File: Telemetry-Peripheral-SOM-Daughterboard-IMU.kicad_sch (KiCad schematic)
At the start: 8 parts, among them J1 Conn_02x10_Odd_Even, U1 LSM6DSV

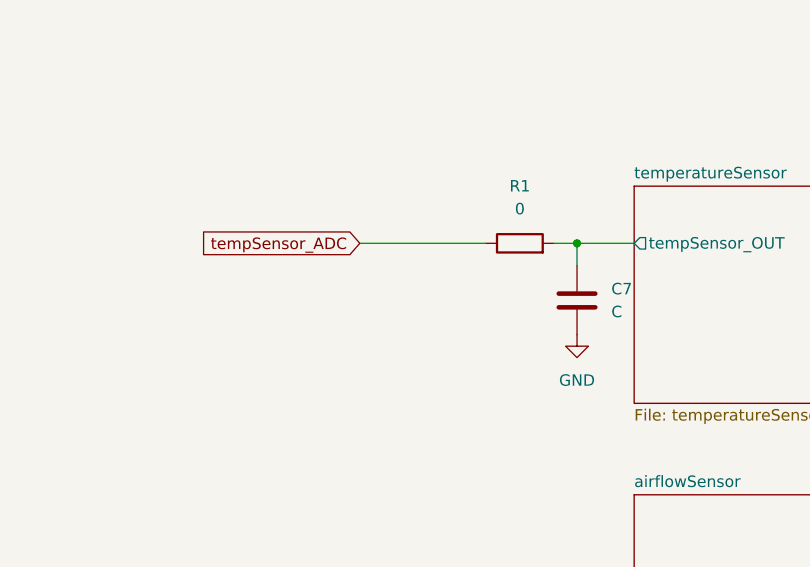
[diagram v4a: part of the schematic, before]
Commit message: temperatureSensor fix
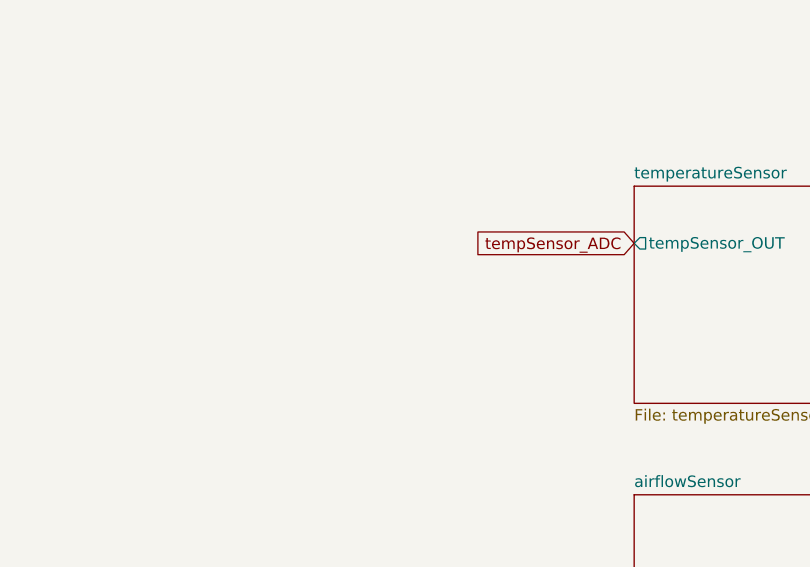
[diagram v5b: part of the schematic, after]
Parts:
- removed C7: C, symbol Device:C
- removed R1: 0, symbol Device:R
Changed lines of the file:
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@@
   (junction (at 87.63 40.64) (diameter 0) (color 0 0 0 0)
-  )
-  (junction (at 119.38 127) (diameter 0) (color 0 0 0 0)
   )
   (junction (at 80.01 38.1) (diameter 0) (color 0 0 0 0)
@@
     (stroke (width 0) (type default))
   )
-  (wire (pts (xy 119.38 127) (xy 119.38 129.54))
-    (stroke (width 0) (type default))
-  )
   (wire (pts (xy 254 45.72) (xy 257.81 45.72))
     (stroke (width 0) (type default))
@@
     (stroke (width 0) (type default))
   )
-  (wire (pts (xy 116.84 127) (xy 119.38 127))
-    (stroke (width 0) (type default))
-  )
   (wire (pts (xy 254 30.48) (xy 257.81 30.48))
     (stroke (width 0) (type default))
@@
   )
   (wire (pts (xy 254 43.18) (xy 257.81 43.18))
-    (stroke (width 0) (type default))
-  )
-  (wire (pts (xy 95.25 127) (xy 109.22 127))
-    (stroke (width 0) (type default))
-  )
-  (wire (pts (xy 119.38 127) (xy 125.73 127))
     (stroke (width 0) (type default))
   )
@@
     (effects (font (size 1.27 1.27)) (justify right bottom))
   )
-  (global_label "tempSensor_ADC" (shape input) (at 95.25 127 180) (fields_autoplaced)
+  (global_label "tempSensor_ADC" (shape input) (at 125.73 127 180) (fields_autoplaced)
     (effects (font (size 1.27 1.27)) (justify right))
-    (property "Intersheetrefs" "${INTERSHEET_REFS}" (at 76.6016 127 0)
+    (property "Intersheetrefs" "${INTERSHEET_REFS}" (at 107.0816 127 0)
       (effects (font (size 1.27 1.27)) (justify right) hide)
     )
@@
         (path "/d5ebd247-5a7c-47c2-8aee-beabaef72d6d"
           (reference "#PWR043") (unit 1)
-        )
-      )
-    )
-  )
-  (symbol (lib_id "Device:C") (at 119.38 133.35 0) (unit 1)
-    (in_bom yes) (on_board yes) (dnp no) (fields_autoplaced)
-    (property "Reference" "C7" (at 123.19 132.08 0)
-      (effects (font (size 1.27 1.27)) (justify left))
-    )
-    (property "Value" "C" (at 123.19 134.62 0)
-      (effects (font (size 1.27 1.27)) (justify left))
-    )
-    (property "Footprint" "" (at 120.3452 137.16 0)
-      (effects (font (size 1.27 1.27)) hide)
-    )
-    (property "Datasheet" "~" (at 119.38 133.35 0)
-      (effects (font (size 1.27 1.27)) hide)
-    )
-    (pin "1")
-    (pin "2")
-    (instances
-      (project "Telemetry-Peripheral-SOM-Daughterboard-IMU"
-        (path "/637f68f0-cb9c-412a-8573-5d8e7ef6d8a2"
-          (reference "C7") (unit 1)
         )
       )
@@
     )
   )
-  (symbol (lib_id "power:GND") (at 119.38 137.16 0) (unit 1)
-    (in_bom yes) (on_board yes) (dnp no) (fields_autoplaced)
-    (property "Reference" "#PWR017" (at 119.38 143.51 0)
-      (effects (font (size 1.27 1.27)) hide)
-    )
-    (property "Value" "GND" (at 119.38 142.24 0)
-      (effects (font (size 1.27 1.27)))
-    )
-    (property "Footprint" "" (at 119.38 137.16 0)
-      (effects (font (size 1.27 1.27)) hide)
-    )
-    (property "Datasheet" "" (at 119.38 137.16 0)
-      (effects (font (size 1.27 1.27)) hide)
-    )
-    (pin "1")
-    (instances
-      (project "Telemetry-Peripheral-SOM-Daughterboard-IMU"
-        (path "/637f68f0-cb9c-412a-8573-5d8e7ef6d8a2"
-          (reference "#PWR017") (unit 1)
-        )
-      )
-    )
-  )
   (symbol (lib_id "Device:C_Small") (at 80.01 41.91 0) (unit 1)
     (in_bom yes) (on_board yes) (dnp no)
@@
         )
       )
-    )
-  )
-  (symbol (lib_id "Device:R") (at 113.03 127 90) (unit 1)
-    (in_bom yes) (on_board yes) (dnp no) (fields_autoplaced)
-    (property "Reference" "R1" (at 113.03 120.65 90)
-      (effects (font (size 1.27 1.27)))
-    )
-    (property "Value" "0" (at 113.03 123.19 90)
-      (effects (font (size 1.27 1.27)))
-    )
-    (property "Footprint" "" (at 113.03 128.778 90)
-      (effects (font (size 1.27 1.27)) hide)
-    )
-    (property "Datasheet" "~" (at 113.03 127 0)
-      (effects (font (size 1.27 1.27)) hide)
-    )
-    (pin "1")
-    (pin "2")
-    (instances
-      (project "Telemetry-Peripheral-SOM-Daughterboard-IMU"
-        (path "/637f68f0-cb9c-412a-8573-5d8e7ef6d8a2"
-          (reference "R1") (unit 1)
-        )
-      )

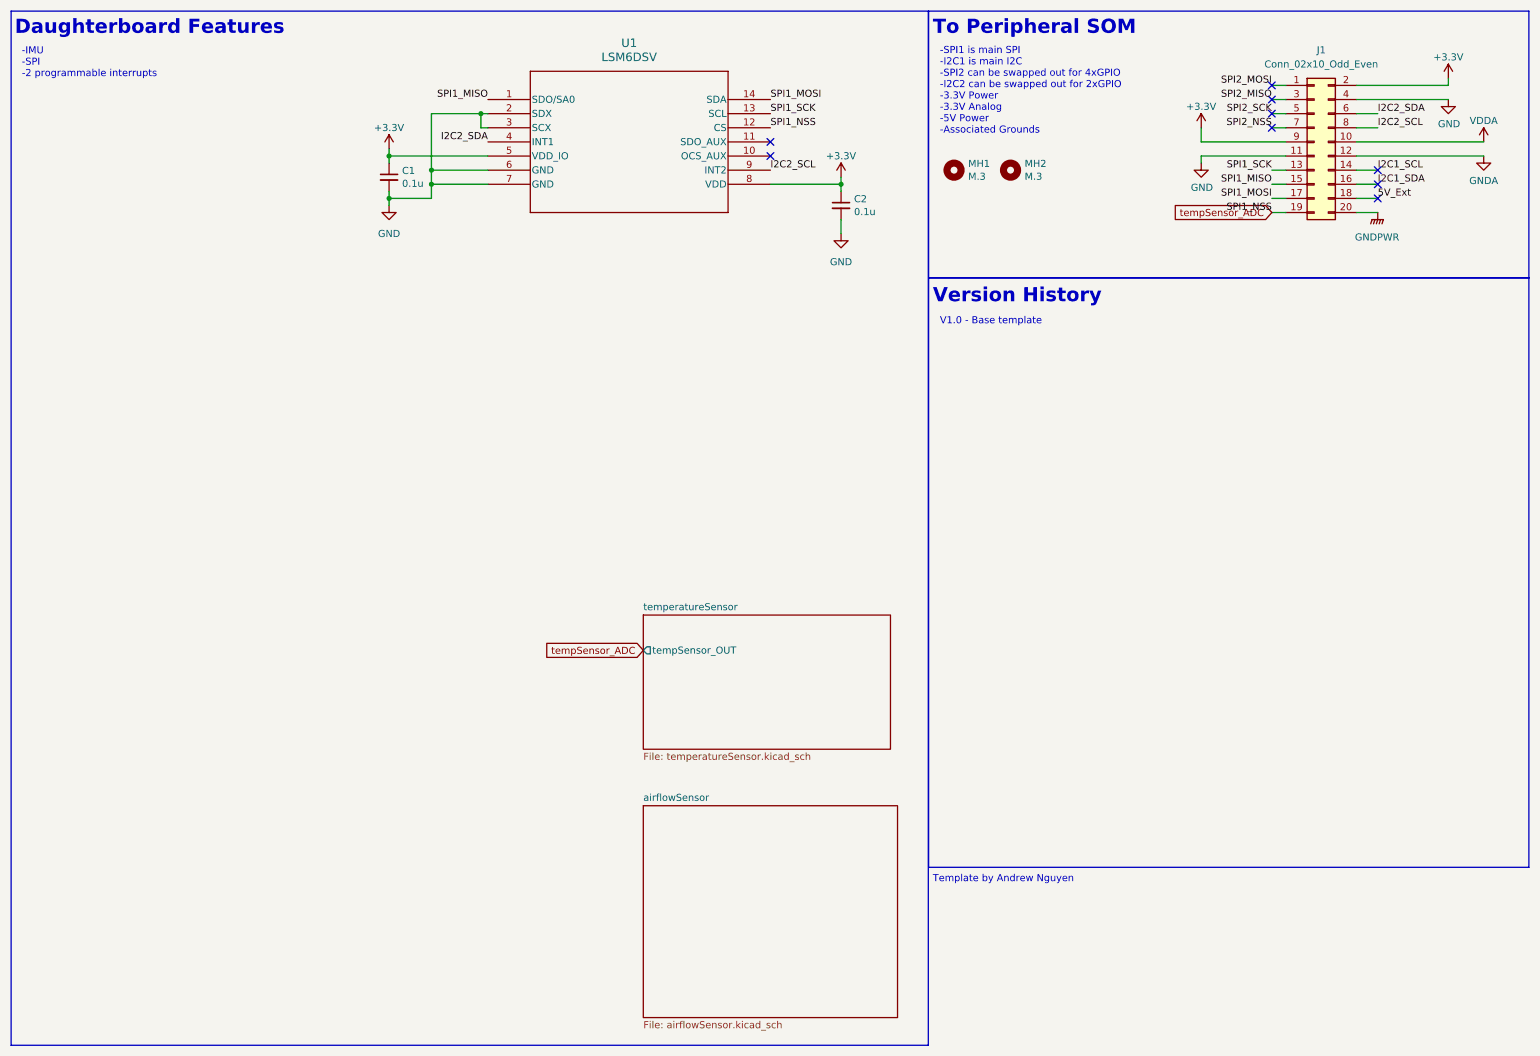
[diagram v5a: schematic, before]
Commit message: connected airflow and temperature sensors to connector J1
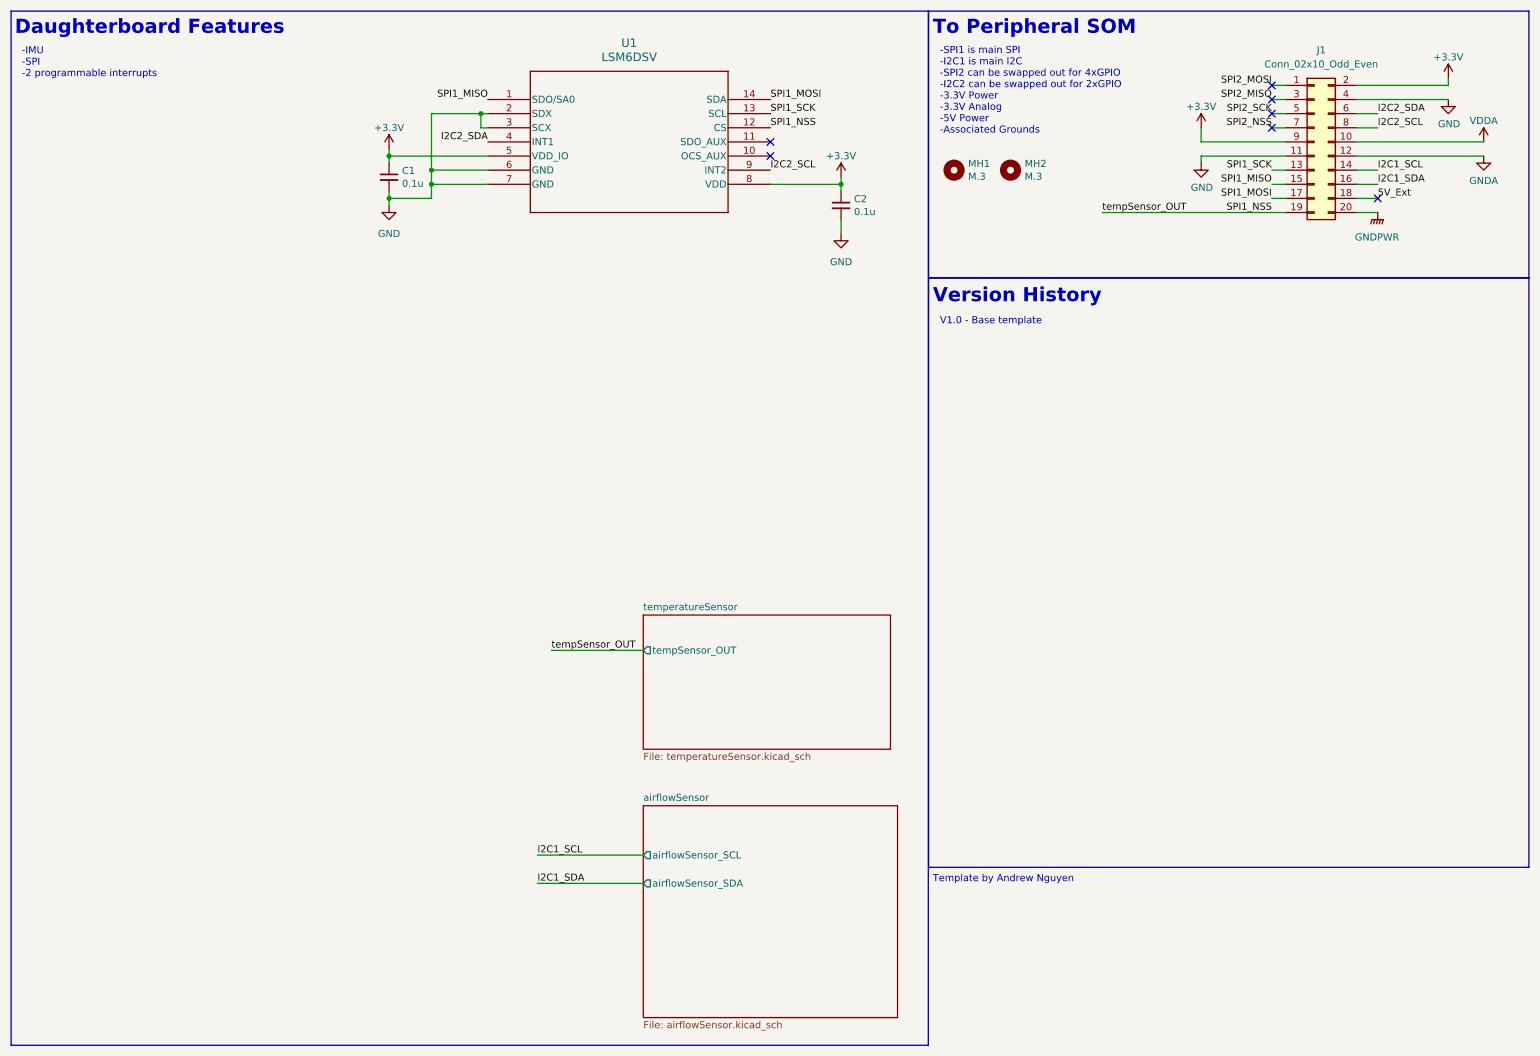
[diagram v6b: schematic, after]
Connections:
- net tempSensor_ADC renamed SPI1_NSS
- no-connect marks 9 -> 7
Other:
- sheet airflowSensor ports: added airflowSensor_SCL, airflowSensor_SDA; removed none
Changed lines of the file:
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@@
   (no_connect (at 238.76 27.94))
   (no_connect (at 148.59 35.56))
-  (no_connect (at 257.81 43.18))
   (no_connect (at 238.76 33.02))
   (no_connect (at 238.76 25.4))
-  (no_connect (at 257.81 40.64))
   (no_connect (at 238.76 30.48))
   (wire (pts (xy 254 27.94) (xy 270.51 27.94))
@@
     (stroke (width 0) (type default))
   )
+  (wire (pts (xy 109.22 127) (xy 125.73 127))
+    (stroke (width 0) (type default))
+  )
   (wire (pts (xy 254 30.48) (xy 257.81 30.48))
     (stroke (width 0) (type default))
@@
     (stroke (width 0) (type default))
   )
-  (wire (pts (xy 238.76 48.26) (xy 241.3 48.26))
+  (wire (pts (xy 208.28 48.26) (xy 241.3 48.26))
     (stroke (width 0) (type default))
   )
@@
     (stroke (width 0) (type default))
   )
+  (wire (pts (xy 106.68 168.91) (xy 125.73 168.91))
+    (stroke (width 0) (type default))
+  )
   (wire (pts (xy 254 33.02) (xy 257.81 33.02))
     (stroke (width 0) (type default))
@@
   )
   (wire (pts (xy 80.01 44.45) (xy 80.01 45.72))
+    (stroke (width 0) (type default))
+  )
+  (wire (pts (xy 106.68 163.83) (xy 125.73 163.83))
     (stroke (width 0) (type default))
   )
@@
     (effects (font (size 1.27 1.27)) (justify right bottom))
   )
+  (label "tempSensor_OUT" (at 109.22 127 0) (fields_autoplaced)
+    (effects (font (size 1.27 1.27)) (justify left bottom))
+  )
   (label "SPI1_MISO" (at 238.76 43.18 180) (fields_autoplaced)
     (effects (font (size 1.27 1.27)) (justify right bottom))
@@
     (effects (font (size 1.27 1.27)) (justify left bottom))
   )
+  (label "tempSensor_OUT" (at 208.28 48.26 0) (fields_autoplaced)
+    (effects (font (size 1.27 1.27)) (justify left bottom))
+  )
   (label "SPI2_MISO" (at 238.76 27.94 180) (fields_autoplaced)
     (effects (font (size 1.27 1.27)) (justify right bottom))
@@
     (effects (font (size 1.27 1.27)) (justify left bottom))
   )
+  (label "I2C1_SDA" (at 106.68 168.91 0) (fields_autoplaced)
+    (effects (font (size 1.27 1.27)) (justify left bottom))
+  )
+  (label "I2C1_SCL" (at 106.68 163.83 0) (fields_autoplaced)
+    (effects (font (size 1.27 1.27)) (justify left bottom))
+  )
   (label "SPI1_SCK" (at 238.76 40.64 180) (fields_autoplaced)
     (effects (font (size 1.27 1.27)) (justify right bottom))
@@
   (label "SPI2_NSS" (at 238.76 33.02 180) (fields_autoplaced)
     (effects (font (size 1.27 1.27)) (justify right bottom))
-  )
-  (global_label "tempSensor_ADC" (shape input) (at 125.73 127 180) (fields_autoplaced)
-    (effects (font (size 1.27 1.27)) (justify right))
-    (property "Intersheetrefs" "${INTERSHEET_REFS}" (at 107.0816 127 0)
-      (effects (font (size 1.27 1.27)) (justify right) hide)
-    )
-  )
-  (global_label "tempSensor_ADC" (shape input) (at 238.76 48.26 180) (fields_autoplaced)
-    (effects (font (size 1.27 1.27)) (justify right))
-    (property "Intersheetrefs" "${INTERSHEET_REFS}" (at 220.1116 48.26 0)
-      (effects (font (size 1.27 1.27)) (justify right) hide)
-    )
   )
   (symbol (lib_id "power:+3.3V") (at 80.01 36.83 0) (unit 1)
@@
       (effects (font (size 1.27 1.27)) (justify left top))
     )
-    (instances
+    (pin "airflowSensor_SDA" output (at 125.73 168.91 180)
+      (effects (font (size 1.27 1.27)) (justify left))
+    )
+    (pin "airflowSensor_SCL" output (at 125.73 163.83 180)
+      (effects (font (size 1.27 1.27)) (justify left))
+    )
+    (instances

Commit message: fixed errors
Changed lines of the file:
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@@
-    (stroke (width 0) (type default))
-  )
-  (wire (pts (xy 208.28 48.26) (xy 241.3 48.26))
     (stroke (width 0) (type default))
   )
@@
   )
   (wire (pts (xy 238.76 27.94) (xy 241.3 27.94))
+    (stroke (width 0) (type default))
+  )
+  (wire (pts (xy 238.76 48.26) (xy 241.3 48.26))
     (stroke (width 0) (type default))
   )
@@
     (effects (font (size 1.27 1.27)) (justify right bottom))
   )
-  (label "tempSensor_OUT" (at 109.22 127 0) (fields_autoplaced)
+  (label "SPI1_NSS" (at 109.22 127 0) (fields_autoplaced)
     (effects (font (size 1.27 1.27)) (justify left bottom))
   )
@@
     (effects (font (size 1.27 1.27)) (justify left bottom))
   )
-  (label "tempSensor_OUT" (at 208.28 48.26 0) (fields_autoplaced)
-    (effects (font (size 1.27 1.27)) (justify left bottom))
-  )

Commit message: fix
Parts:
- U1: footprint UTSVT_ICs:LGA14-L_2P59X3P1X0P5_STM -> UTSVT_Special:LGA14-L_2P59X3P1X0P5_STM
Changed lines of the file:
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@@
       (effects (font (size 1.524 1.524)))
     )
-    (property "Footprint" "UTSVT_ICs:LGA14-L_2P59X3P1X0P5_STM" (at 97.79 27.94 0)
+    (property "Footprint" "UTSVT_Special:LGA14-L_2P59X3P1X0P5_STM" (at 97.79 27.94 0)
       (effects (font (size 1.27 1.27) italic) hide)
     )
